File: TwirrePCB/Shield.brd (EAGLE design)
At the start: 96.2 x 53.6 mm, 60 parts, among them Q1 BSS138, Q2 BSS138, T2 BC847, U1 ARDUINO-MEGAPRO

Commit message: Change Transistors for FMMT491A and FMMT591A
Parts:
- removed T1: (no value), transistor:SOT23-BEC
- removed T2: BC847, transistor:SOT23
- added T3: FMMT591A, transistor:SOT23-BCE
- added T4: FMMT491A, transistor:SOT23-BEC
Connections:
- net +3V3: now also T3.E; no longer T1.E
- net GND: now also T4.E; no longer T2.2
- net N$1: now also T3.B; no longer T1.B
- net N$2: now also T4.C; no longer T2.3
- net N$3: now also T4.B; no longer T2.1
- net SPI_VIN: now also T3.C; no longer T1.C
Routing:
- net +3V3: track 247.9 -> 251.4 mm, vias 7 -> 8
- net N$1: track 4.68 -> 5.40 mm
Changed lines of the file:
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@@
 <grid distance="0.0125" unitdist="inch" unit="inch" style="lines" multiple="1" display="no" altdistance="0.025" altunitdist="inch" altunit="inch"/>
 <layers>
-<layer number="1" name="Top" color="4" fill="1" visible="no" active="yes"/>
-<layer number="16" name="Bottom" color="1" fill="1" visible="no" active="yes"/>
+<layer number="1" name="Top" color="4" fill="1" visible="yes" active="yes"/>
+<layer number="16" name="Bottom" color="1" fill="1" visible="yes" active="yes"/>
 <layer number="17" name="Pads" color="2" fill="1" visible="yes" active="yes"/>
 <layer number="18" name="Vias" color="2" fill="1" visible="yes" active="yes"/>
@@
 <elements>
 <element name="U1" library="Arduino-Boards" package="ARDUINO_MEGA-PRO-3.3V" value="ARDUINO-MEGAPRO" x="0" y="0"/>
-<element name="T1" library="transistor" package="SOT23-BEC" value="" x="32.0675" y="30.7975" smashed="yes" rot="R90">
-<attribute name="VALUE" x="35.2425" y="28.8925" size="1.27" layer="27" rot="R90"/>
-</element>
-<element name="T2" library="transistor" package="SOT23" value="BC847" x="32.0675" y="25.0825" smashed="yes" rot="R90">
-<attribute name="VALUE" x="35.2425" y="23.1775" size="1.27" layer="27" rot="R90"/>
-</element>
 <element name="R1" library="resistor" package="R0805" value="10k" x="35.8775" y="30.7975" smashed="yes" rot="R90">
 <attribute name="VALUE" x="38.4175" y="30.1625" size="1.27" layer="27" rot="R90"/>
@@
 <element name="C2" library="resistor" package="153CLV-0605" value="47uF" x="25.4" y="26.3525" rot="R90"/>
 <element name="U$25" library="Arduino-Boards" package="IDC-8WAY" value="IDC-8WAY" x="45.4025" y="26.9875"/>
+<element name="T3" library="transistor" package="SOT23-BCE" value="FMMT591A " x="32.0675" y="31.115" rot="R90"/>
+<element name="T4" library="transistor" package="SOT23-BEC" value="FMMT491A " x="32.0675" y="24.765" rot="R90"/>
 </elements>
 <signals>
@@
 <contactref element="U1" pad="GND@2"/>
 <contactref element="U1" pad="SPI_GND"/>
-<contactref element="T2" pad="2"/>
 <contactref element="R4" pad="2"/>
 <contactref element="LED1" pad="C"/>
@@
 <wire x1="34.29" y1="26.3525" x2="33.9725" y2="26.035" width="0.3048" layer="1"/>
 <wire x1="33.9725" y1="26.035" x2="33.17" y2="26.035" width="0.3048" layer="1"/>
-<wire x1="33.17" y1="26.035" x2="33.1675" y2="26.0325" width="0.3048" layer="1"/>
 <wire x1="38.4175" y1="26.0325" x2="38.4175" y2="27.94" width="0.3048" layer="1"/>
 <wire x1="1.533025" y1="21.59" x2="0.635" y2="22.488025" width="0.6096" layer="16"/>
@@
 <wire x1="39.6875" y1="37.1475" x2="39.37" y2="37.465" width="0.3048" layer="16"/>
 <wire x1="42.1675" y1="46.4375" x2="42.1675" y2="39.77" width="0.6096" layer="1"/>
+<contactref element="T4" pad="E"/>
+<wire x1="33.1675" y1="25.715" x2="33.17" y2="26.0325" width="0.3048" layer="1"/>
+<wire x1="33.17" y1="26.0325" x2="33.17" y2="26.035" width="0.3048" layer="1"/>
 </signal>
 <signal name="SPI_VIN">
-<contactref element="T1" pad="C"/>
 <contactref element="R5" pad="1"/>
-<wire x1="30.9675" y1="30.7975" x2="30.9675" y2="32.8725" width="0.3048" layer="1"/>
 <wire x1="31.4325" y1="33.3375" x2="41.91" y2="33.3375" width="0.3048" layer="16"/>
 <via x="31.4325" y="33.3375" extent="1-16" drill="0.6" shape="square"/>
 <wire x1="31.4325" y1="33.3375" x2="31.4325" y2="34.925" width="0.3048" layer="1"/>
 <wire x1="31.4325" y1="34.925" x2="31.7525" y2="34.925" width="0.3048" layer="1"/>
-<wire x1="30.9675" y1="32.8725" x2="31.4325" y2="33.3375" width="0.3048" layer="1"/>
 <contactref element="U$25" pad="6"/>
 <wire x1="46.6725" y1="25.7175" x2="45.4025" y2="26.9875" width="0.3048" layer="1"/>
@@
 <wire x1="44.2577375" y1="33.3375" x2="41.91" y2="33.3375" width="0.3048" layer="1"/>
 <via x="41.91" y="33.3375" extent="1-16" drill="0.6" shape="square"/>
+<contactref element="T3" pad="C"/>
+<wire x1="33.1675" y1="32.065" x2="33.02" y2="32.065" width="0.3048" layer="1"/>
+<wire x1="33.02" y1="32.065" x2="31.7475" y2="33.3375" width="0.3048" layer="1"/>
+<wire x1="31.7475" y1="33.3375" x2="31.4325" y2="33.3375" width="0.3048" layer="1"/>
 </signal>
 <signal name="FLIR_PWR">
@@
 </signal>
 <signal name="N$1">
-<contactref element="T1" pad="B"/>
 <contactref element="R1" pad="1"/>
 <contactref element="R2" pad="2"/>
+<wire x1="33.0175" y1="27.94" x2="33.0175" y2="30.165" width="0.3048" layer="1"/>
+<contactref element="T3" pad="B"/>
 <wire x1="35.8775" y1="29.8475" x2="33.1675" y2="29.8475" width="0.3048" layer="1"/>
-<wire x1="33.0175" y1="27.94" x2="33.0175" y2="29.6975" width="0.3048" layer="1"/>
-<wire x1="33.0175" y1="29.6975" x2="33.1675" y2="29.8475" width="0.3048" layer="1"/>
+<wire x1="33.1675" y1="29.8475" x2="33.1675" y2="30.165" width="0.3048" layer="1"/>
+<wire x1="33.1675" y1="30.165" x2="33.0175" y2="30.165" width="0.3048" layer="1"/>
 </signal>
 <signal name="N$2">
-<contactref element="T2" pad="3"/>
 <contactref element="R2" pad="1"/>
-<wire x1="31.1175" y1="27.94" x2="31.1175" y2="25.2325" width="0.3048" layer="1"/>
-<wire x1="31.1175" y1="25.2325" x2="30.9675" y2="25.0825" width="0.3048" layer="1"/>
+<wire x1="31.1175" y1="27.94" x2="31.1175" y2="24.765" width="0.3048" layer="1"/>
+<contactref element="T4" pad="C"/>
+<wire x1="30.9675" y1="24.765" x2="31.1175" y2="24.765" width="0.3048" layer="1"/>
 </signal>
 <signal name="N$3">
 <contactref element="R3" pad="1"/>
-<contactref element="T2" pad="1"/>
 <contactref element="R4" pad="1"/>
-<wire x1="33.1675" y1="24.1325" x2="33.6575" y2="24.1325" width="0.3048" layer="1"/>
 <wire x1="33.6575" y1="24.1325" x2="35.5575" y2="26.0325" width="0.3048" layer="1"/>
 <wire x1="35.5575" y1="26.0325" x2="35.8775" y2="26.0325" width="0.3048" layer="1"/>
@@
 <wire x1="37.5965125" y1="24.4475" x2="38.4175" y2="24.4475" width="0.3048" layer="1"/>
 <wire x1="38.4175" y1="24.4475" x2="38.4175" y2="24.1325" width="0.3048" layer="1"/>
+<contactref element="T4" pad="B"/>
+<wire x1="33.1675" y1="23.815" x2="33.6575" y2="23.815" width="0.3048" layer="1"/>
+<wire x1="33.6575" y1="23.815" x2="33.6575" y2="24.1325" width="0.3048" layer="1"/>
 </signal>
 <signal name="N$4">
@@
 </signal>
 <signal name="+3V3">
-<contactref element="T1" pad="E"/>
 <contactref element="R1" pad="2"/>
 <contactref element="Q1" pad="1"/>
@@
 <wire x1="41.1979625" y1="6.985" x2="42.545" y2="8.3320375" width="0.6096" layer="16"/>
 <wire x1="42.545" y1="8.3320375" x2="42.545" y2="19.685" width="0.6096" layer="16"/>
-<wire x1="35.8775" y1="31.7475" x2="33.1675" y2="31.7475" width="0.3048" layer="1"/>
 <wire x1="35.8775" y1="31.7475" x2="40.64" y2="31.7475" width="0.3048" layer="1"/>
 <wire x1="40.64" y1="31.7475" x2="40.9575" y2="31.4325" width="0.3048" layer="1"/>
@@
 <wire x1="41.275" y1="23.1775" x2="41.275" y2="20.32" width="0.3048" layer="16"/>
 <contactref element="SV2" pad="7"/>
-<wire x1="25.0825" y1="34.925" x2="25.0825" y2="20.32" width="0.6096" layer="16"/>
+<wire x1="25.0825" y1="34.925" x2="25.0825" y2="31.4325" width="0.6096" layer="16"/>
+<wire x1="25.0825" y1="31.4325" x2="25.0825" y2="20.32" width="0.6096" layer="16"/>
 <wire x1="25.0825" y1="20.32" x2="23.8125" y2="19.05" width="0.6096" layer="16"/>
 <wire x1="23.8125" y1="19.05" x2="23.8125" y2="5.3975" width="0.6096" layer="16"/>
@@
 <wire x1="25.4" y1="29.0525" x2="25.0825" y2="30.005" width="0.6096" layer="1"/>
 <wire x1="25.0825" y1="30.005" x2="25.0825" y2="34.925" width="0.6096" layer="1"/>
+<contactref element="T3" pad="E"/>
+<wire x1="30.9675" y1="31.115" x2="28.8925" y2="31.115" width="0.3048" layer="1"/>
+<via x="28.8925" y="31.115" extent="1-16" drill="0.6" shape="square"/>
+<wire x1="28.8925" y1="31.115" x2="25.0825" y2="31.115" width="0.3048" layer="16"/>
+<wire x1="25.0825" y1="31.115" x2="25.0825" y2="31.4325" width="0.3048" layer="16"/>
 </signal>
 <signal name="SCL_LS">

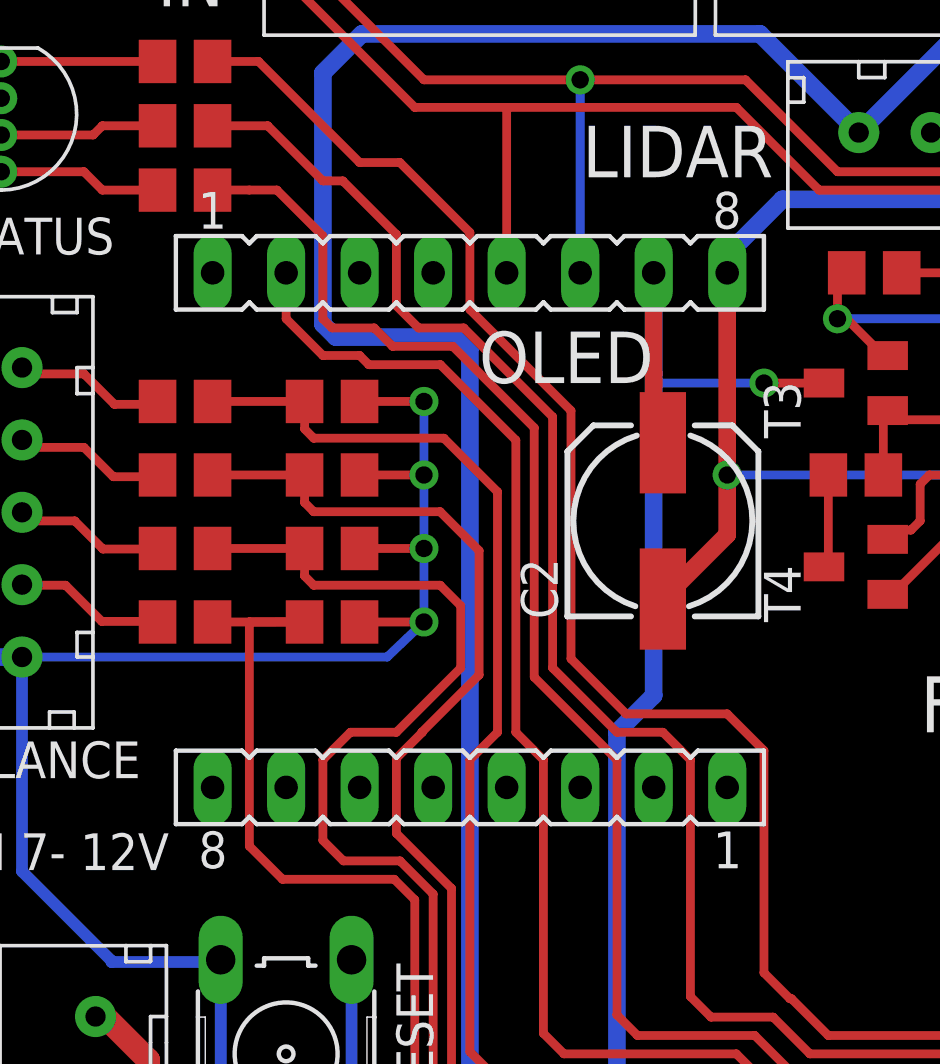
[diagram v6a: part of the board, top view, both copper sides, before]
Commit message: Modify OLED and Servo Headers
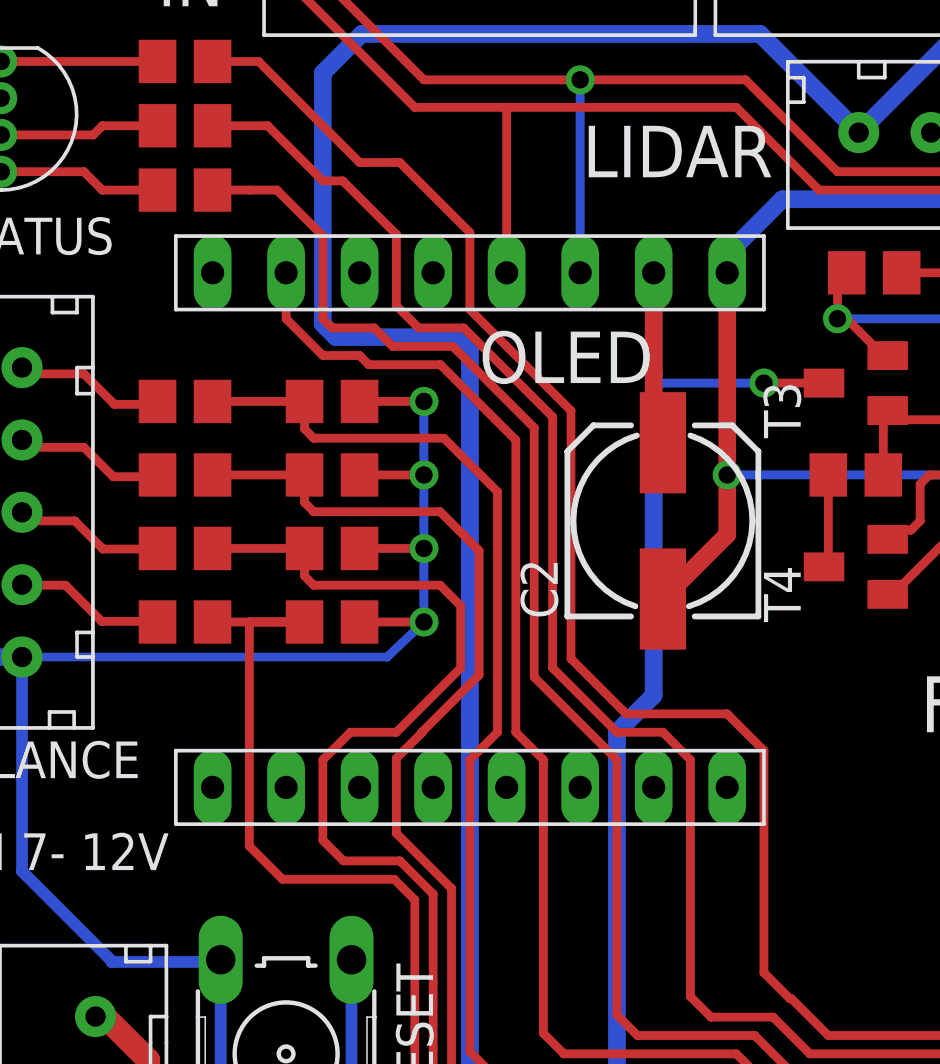
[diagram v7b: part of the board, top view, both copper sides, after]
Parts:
- removed SV2, SV3: (no value), con-lsta:FE08
- added U$26, U$27: OLEDHEADER, Arduino-Boards:OLEDHEADER
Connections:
- net +3V3: now also U$26.P$7; no longer SV2.7
- net GND: now also U$26.P$8; no longer SV2.8
- net N$24: now also U$26.P$2; no longer SV2.2
- net SCL_LS: now also U$26.P$5; no longer SV2.5
- net SDA_LS: now also U$26.P$6; no longer SV2.6
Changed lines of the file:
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@@
 <element name="U$12" library="Arduino-Boards" package="JST-5" value="LIDAR" x="38.4175" y="39.37" rot="R180"/>
 <element name="U$13" library="Arduino-Boards" package="JST-5" value="LIDAR" x="2.8575" y="25.4" rot="R90"/>
-<element name="SV2" library="con-lsta" package="FE08" value="" x="18.7325" y="34.925" smashed="yes">
-<attribute name="MPN" value="" x="18.7325" y="34.925" size="1.778" layer="27" display="off"/>
-<attribute name="OC_FARNELL" value="unknown" x="18.7325" y="34.925" size="1.778" layer="27" display="off"/>
-<attribute name="OC_NEWARK" value="unknown" x="18.7325" y="34.925" size="1.778" layer="27" display="off"/>
-<attribute name="MF" value="" x="18.7325" y="34.925" size="1.778" layer="27" display="off"/>
-<attribute name="VALUE" x="8.5725" y="32.004" size="1.27" layer="27" ratio="10"/>
-</element>
-<element name="SV3" library="con-lsta" package="FE08" value="" x="18.7325" y="17.145" smashed="yes" rot="R180">
-<attribute name="MPN" value="" x="18.7325" y="17.145" size="1.778" layer="27" rot="R180" display="off"/>
-<attribute name="OC_FARNELL" value="unknown" x="18.7325" y="17.145" size="1.778" layer="27" rot="R180" display="off"/>
-<attribute name="OC_NEWARK" value="unknown" x="18.7325" y="17.145" size="1.778" layer="27" rot="R180" display="off"/>
-<attribute name="MF" value="" x="18.7325" y="17.145" size="1.778" layer="27" rot="R180" display="off"/>
-<attribute name="VALUE" x="28.8925" y="20.066" size="1.27" layer="27" ratio="10" rot="R180"/>
-</element>
 <element name="U$14" library="Arduino-Boards" package="JST-3" value="JST-3" x="89.8525" y="22.5425" rot="R90"/>
 <element name="U$15" library="Arduino-Boards" package="JST-3" value="JST-3" x="89.8525" y="12.065" rot="R90"/>
@@
 <element name="T3" library="transistor" package="SOT23-BCE" value="FMMT591A " x="32.0675" y="31.115" rot="R90"/>
 <element name="T4" library="transistor" package="SOT23-BEC" value="FMMT491A " x="32.0675" y="24.765" rot="R90"/>
+<element name="U$26" library="Arduino-Boards" package="OLEDHEADER" value="OLEDHEADER" x="18.7325" y="33.655"/>
+<element name="U$27" library="Arduino-Boards" package="OLEDHEADER" value="OLEDHEADER" x="18.7325" y="18.415" rot="R180"/>
 </elements>
 <signals>
@@
 <wire x1="17.145" y1="22.86" x2="15.875" y2="21.65" width="0.3048" layer="16"/>
 <wire x1="15.875" y1="21.65" x2="3.2575" y2="21.65" width="0.3048" layer="16"/>
-<contactref element="SV2" pad="8"/>
 <wire x1="27.6225" y1="34.925" x2="27.6225" y2="35.56" width="0.6096" layer="16"/>
 <wire x1="27.6225" y1="35.56" x2="29.5275" y2="37.465" width="0.6096" layer="16"/>
@@
 <wire x1="33.1675" y1="25.715" x2="33.17" y2="26.0325" width="0.3048" layer="1"/>
 <wire x1="33.17" y1="26.0325" x2="33.17" y2="26.035" width="0.3048" layer="1"/>
+<contactref element="U$26" pad="P$8"/>
+<contactref element="U$26" pad="P$8"/>
 </signal>
 <signal name="SPI_VIN">
@@
 <wire x1="40.9575" y1="23.495" x2="41.275" y2="23.1775" width="0.3048" layer="16"/>
 <wire x1="41.275" y1="23.1775" x2="41.275" y2="20.32" width="0.3048" layer="16"/>
-<contactref element="SV2" pad="7"/>
 <wire x1="25.0825" y1="34.925" x2="25.0825" y2="31.4325" width="0.6096" layer="16"/>
 <wire x1="25.0825" y1="31.4325" x2="25.0825" y2="20.32" width="0.6096" layer="16"/>
@@
 <wire x1="28.8925" y1="31.115" x2="25.0825" y2="31.115" width="0.3048" layer="16"/>
 <wire x1="25.0825" y1="31.115" x2="25.0825" y2="31.4325" width="0.3048" layer="16"/>
+<contactref element="U$26" pad="P$7"/>
 </signal>
 <signal name="SCL_LS">
@@
 <wire x1="20.0025" y1="40.64" x2="27.94" y2="40.64" width="0.3048" layer="1"/>
 <wire x1="27.94" y1="40.64" x2="30.7975" y2="37.7825" width="0.3048" layer="1"/>
-<contactref element="SV2" pad="5"/>
 <wire x1="20.0025" y1="34.925" x2="20.0025" y2="40.64" width="0.3048" layer="1"/>
 <wire x1="16.8275" y1="40.64" x2="7.3025" y2="50.165" width="0.3048" layer="1"/>
@@
 <wire x1="30.7975" y1="37.7825" x2="42.545" y2="37.7825" width="0.3048" layer="1"/>
 <wire x1="42.545" y1="37.7825" x2="47.3075" y2="33.02" width="0.3048" layer="1"/>
+<contactref element="U$26" pad="P$5"/>
 </signal>
 <signal name="SDA_LS">
@@
 <wire x1="22.5425" y1="41.5925" x2="28.2575" y2="41.5925" width="0.3048" layer="1"/>
 <wire x1="28.2575" y1="41.5925" x2="31.4325" y2="38.4175" width="0.3048" layer="1"/>
-<contactref element="SV2" pad="6"/>
 <wire x1="22.5425" y1="34.925" x2="22.5425" y2="41.5925" width="0.3048" layer="16"/>
 <via x="22.5425" y="41.5925" extent="1-16" drill="0.6" shape="square"/>
@@
 <wire x1="31.4325" y1="38.4175" x2="42.808025" y2="38.4175" width="0.3048" layer="1"/>
 <wire x1="42.808025" y1="38.4175" x2="47.570525" y2="33.655" width="0.3048" layer="1"/>
+<contactref element="U$26" pad="P$6"/>
 </signal>
 <signal name="+5V">
@@
 </signal>
 <signal name="N$24">
-<contactref element="SV2" pad="2"/>
 <contactref element="U1" pad="45"/>
 <wire x1="12.3825" y1="34.925" x2="12.3825" y2="33.3375" width="0.3048" layer="1"/>
@@
 <wire x1="87.9475" y1="18.7325" x2="86.36" y2="20.32" width="0.3048" layer="1"/>
 <wire x1="86.36" y1="20.32" x2="85.09" y2="20.32" width="0.3048" layer="1"/>
+<contactref element="U$26" pad="P$2"/>
 </signal>
 <signal name="N$26">

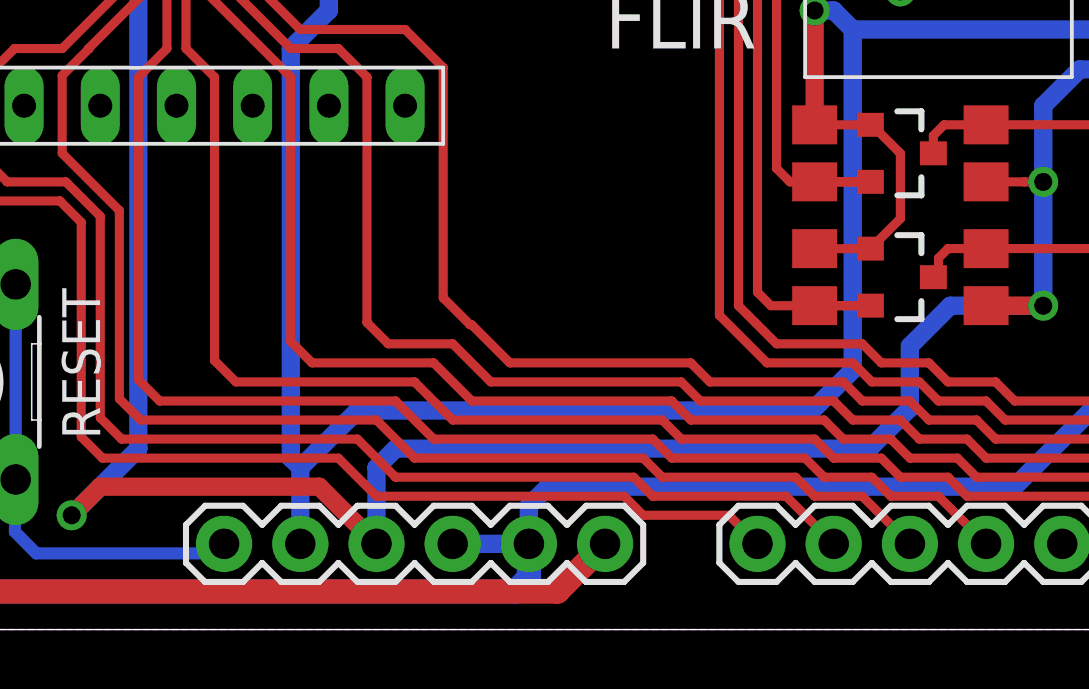
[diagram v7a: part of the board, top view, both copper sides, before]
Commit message: Add NHL Computer Vision Logo
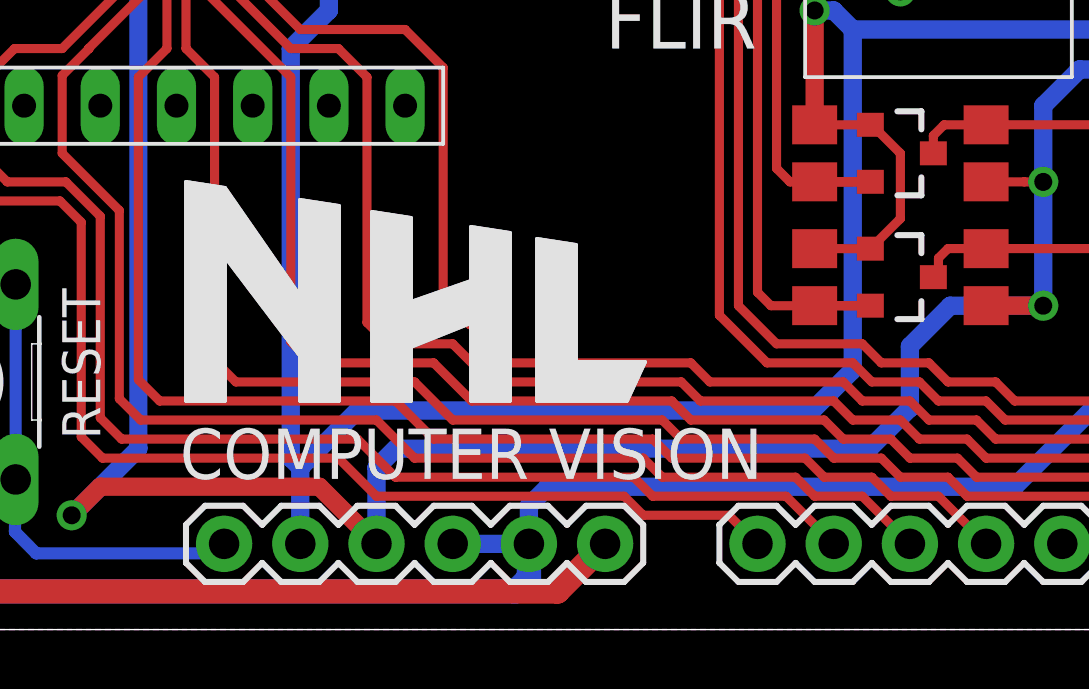
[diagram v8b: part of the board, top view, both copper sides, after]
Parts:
- added U$28: NHLLOGO, Arduino-Boards:NHLLOGO
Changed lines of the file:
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@@
 <grid distance="0.0125" unitdist="inch" unit="inch" style="lines" multiple="1" display="no" altdistance="0.025" altunitdist="inch" altunit="inch"/>
 <layers>
-<layer number="1" name="Top" color="4" fill="1" visible="yes" active="yes"/>
-<layer number="16" name="Bottom" color="1" fill="1" visible="yes" active="yes"/>
+<layer number="1" name="Top" color="4" fill="1" visible="no" active="yes"/>
+<layer number="16" name="Bottom" color="1" fill="1" visible="no" active="yes"/>
 <layer number="17" name="Pads" color="2" fill="1" visible="yes" active="yes"/>
 <layer number="18" name="Vias" color="2" fill="1" visible="yes" active="yes"/>
@@
 <element name="U$26" library="Arduino-Boards" package="OLEDHEADER" value="OLEDHEADER" x="18.7325" y="33.655"/>
 <element name="U$27" library="Arduino-Boards" package="OLEDHEADER" value="OLEDHEADER" x="18.7325" y="18.415" rot="R180"/>
+<element name="U$28" library="Arduino-Boards" package="NHLLOGO" value="NHLLOGO" x="20.32" y="14.605"/>
 </elements>
 <signals>
